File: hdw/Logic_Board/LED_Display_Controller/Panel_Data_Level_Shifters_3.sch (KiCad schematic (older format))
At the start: 43 parts, among them U2801 74LVC1G32, U2802 74HCT541

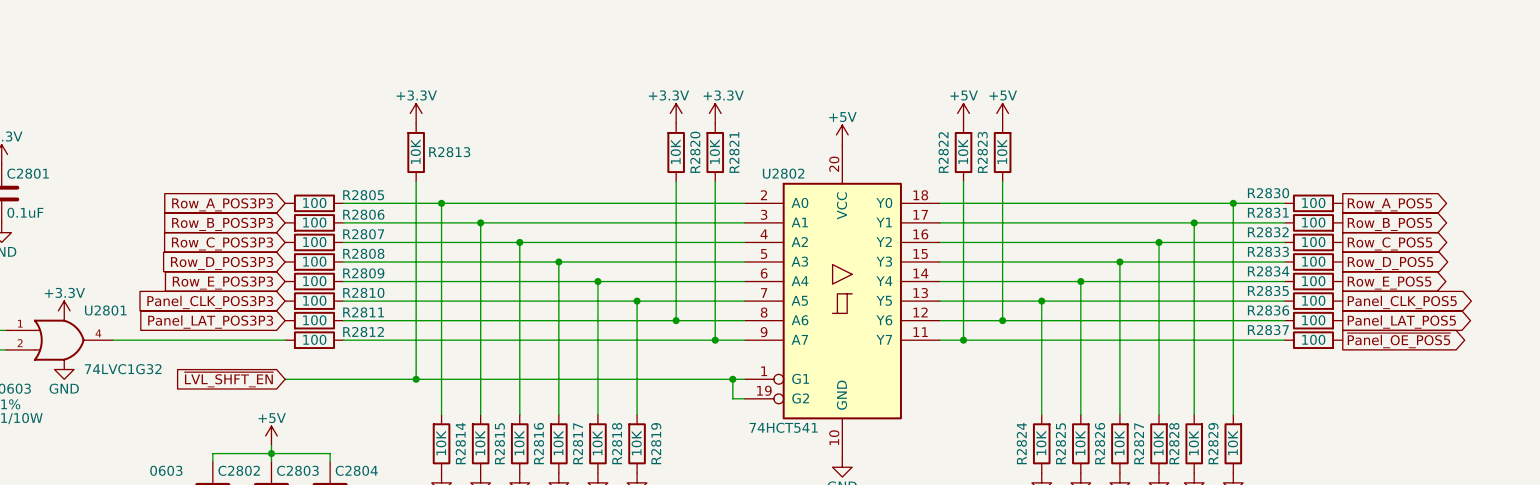
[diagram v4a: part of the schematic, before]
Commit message: Fixed net placement on level shifters, lots of part placements on PCB
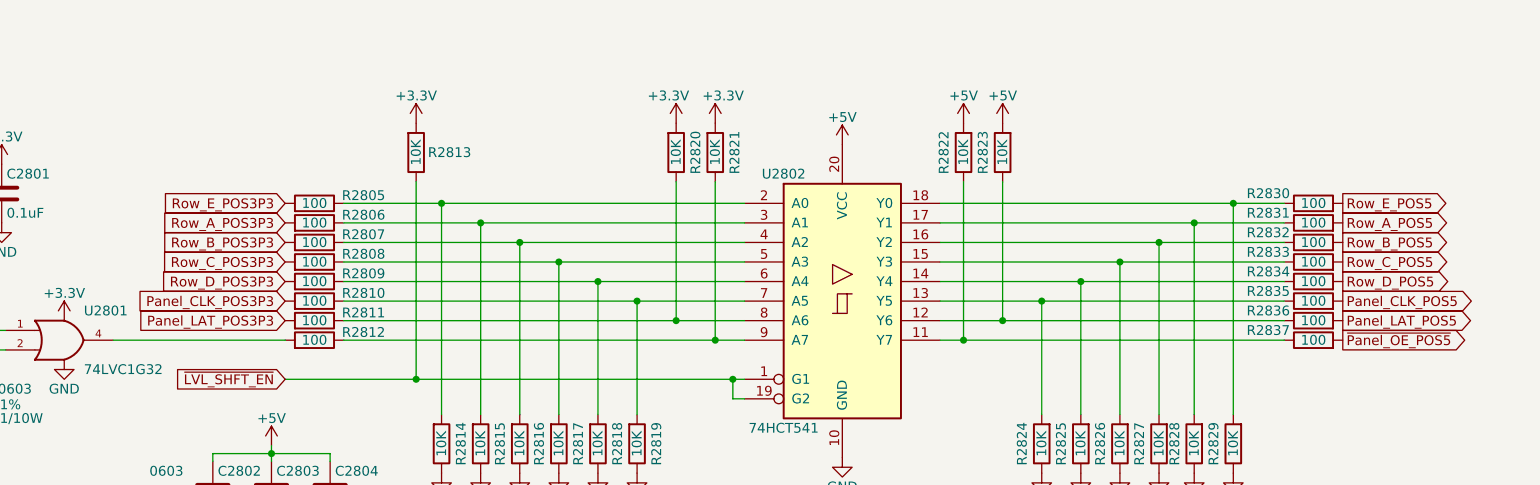
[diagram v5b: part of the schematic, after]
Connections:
- net Row_A_POS3P3: now also R2806.1; no longer R2805.1
- net Row_A_POS5: now also R2831.1; no longer R2830.1
- net Row_B_POS3P3: now also R2807.1; no longer R2806.1
- net Row_B_POS5: now also R2832.1; no longer R2831.1
- net Row_C_POS3P3: now also R2808.1; no longer R2807.1
- net Row_C_POS5: now also R2833.1; no longer R2832.1
- net Row_D_POS3P3: now also R2809.1; no longer R2808.1
- net Row_D_POS5: now also R2834.1; no longer R2833.1
- net Row_E_POS3P3: now also R2805.1; no longer R2809.1
- net Row_E_POS5: now also R2830.1; no longer R2834.1
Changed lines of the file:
@@
 	-1   0    0    -1
 $EndComp
+Text GLabel 9680 3000 2    50   Output ~ 0
+Row_A_POS5
+Text GLabel 9680 3100 2    50   Output ~ 0
+Row_B_POS5
+Text GLabel 9680 3200 2    50   Output ~ 0
+Row_C_POS5
+Text GLabel 9680 3300 2    50   Output ~ 0
+Row_D_POS5
 Text GLabel 9680 2900 2    50   Output ~ 0
-Row_A_POS5
-Text GLabel 9680 3000 2    50   Output ~ 0
-Row_B_POS5
-Text GLabel 9680 3100 2    50   Output ~ 0
-Row_C_POS5
-Text GLabel 9680 3200 2    50   Output ~ 0
-Row_D_POS5
-Text GLabel 9680 3300 2    50   Output ~ 0
 Row_E_POS5
 Text GLabel 9680 3400 2    50   Output ~ 0
@@
 Wire Wire Line
 	4570 3200 5670 3200
+Text GLabel 4270 3000 0    50   Input ~ 0
+Row_A_POS3P3
+Text GLabel 4270 3100 0    50   Input ~ 0
+Row_B_POS3P3
+Text GLabel 4270 3200 0    50   Input ~ 0
+Row_C_POS3P3
+Text GLabel 4270 3300 0    50   Input ~ 0
+Row_D_POS3P3
 Text GLabel 4270 2900 0    50   Input ~ 0
-Row_A_POS3P3
-Text GLabel 4270 3000 0    50   Input ~ 0
-Row_B_POS3P3
-Text GLabel 4270 3100 0    50   Input ~ 0
-Row_C_POS3P3
-Text GLabel 4270 3200 0    50   Input ~ 0
-Row_D_POS3P3
-Text GLabel 4270 3300 0    50   Input ~ 0
 Row_E_POS3P3
 Text GLabel 4270 3400 0    50   Input ~ 0

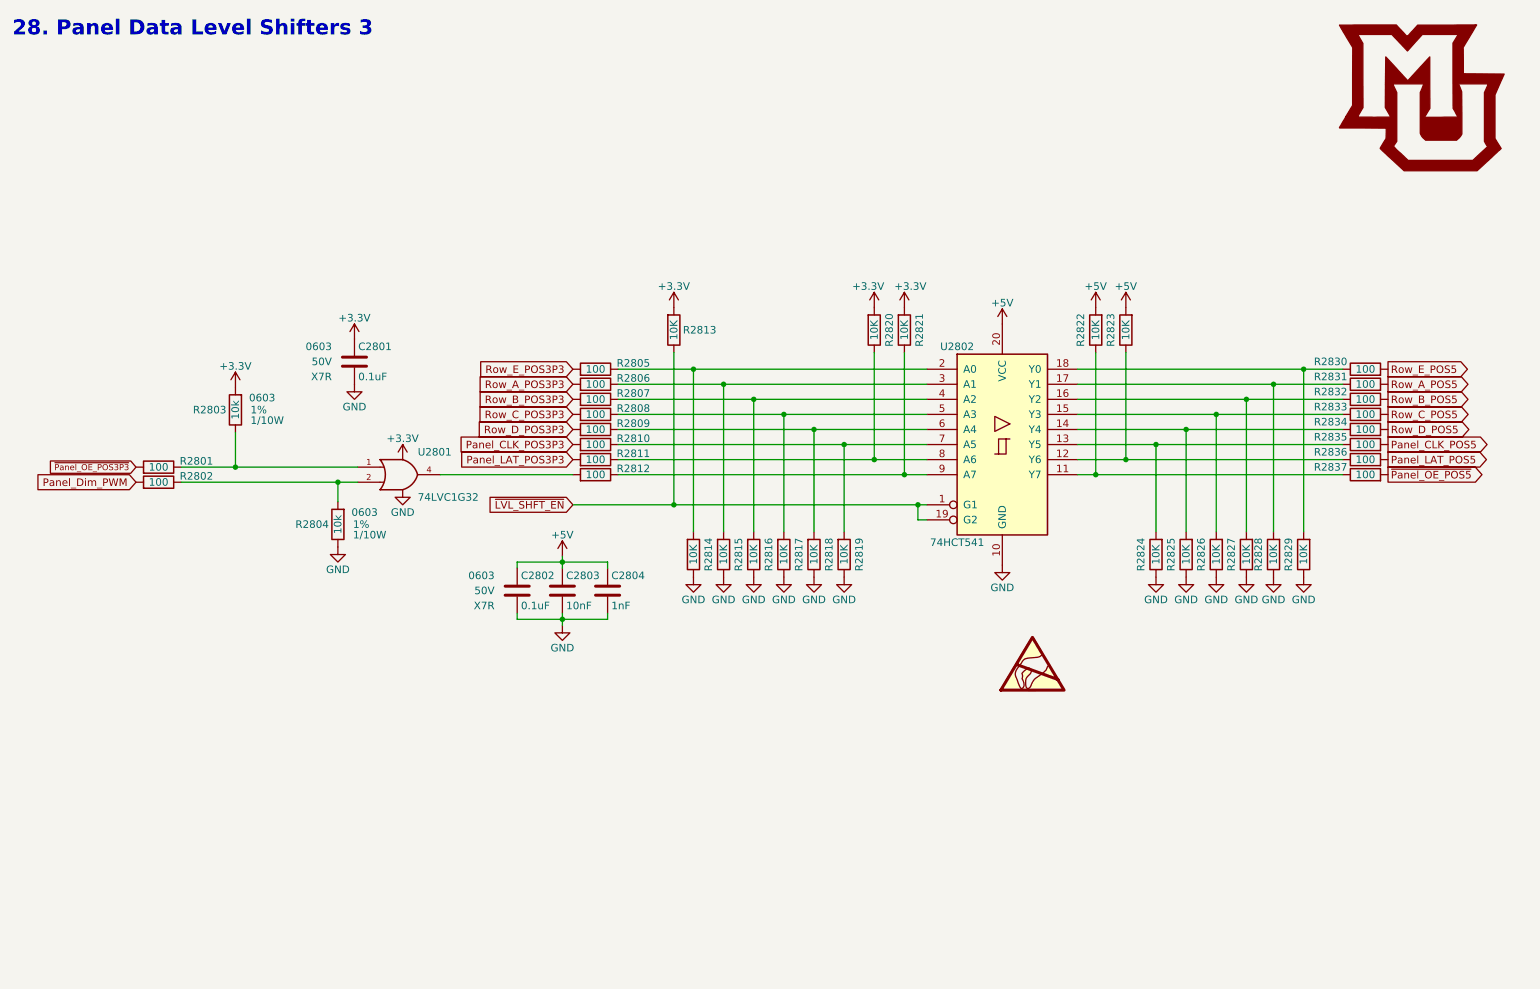
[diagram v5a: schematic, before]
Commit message: Placed more parts, added some labels
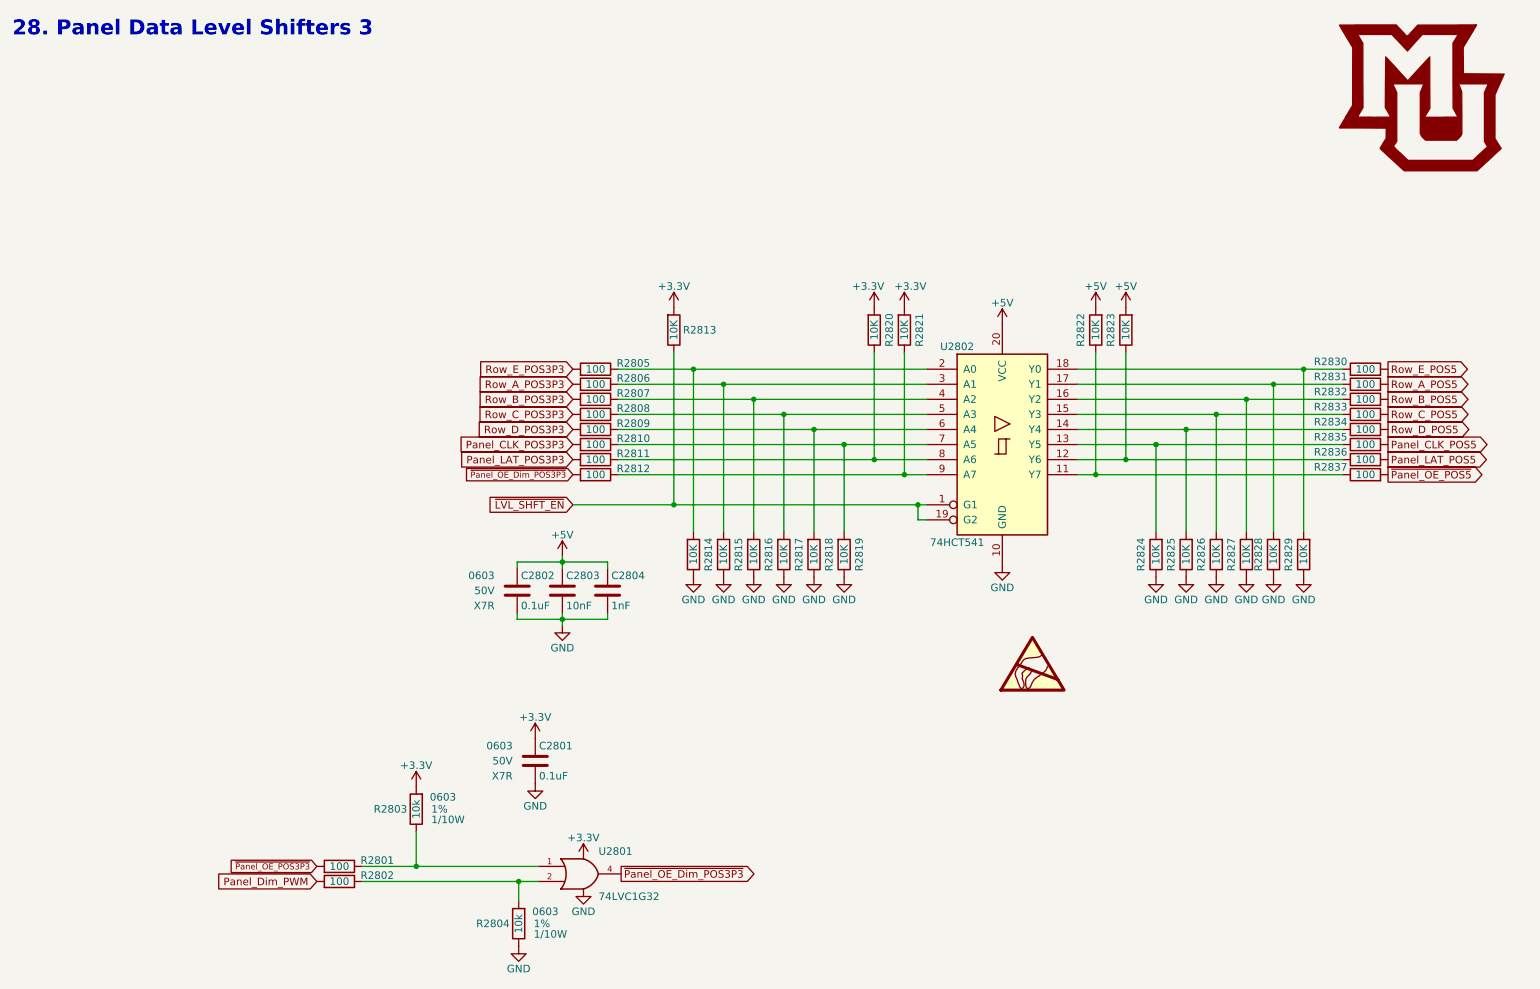
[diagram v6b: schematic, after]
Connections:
- net ~Panel_OE_Dim_POS3P3: now reaches R2812.1, U2801.4
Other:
- moved on the sheet: C2801, R2801, R2802, R2803, R2804, U2801

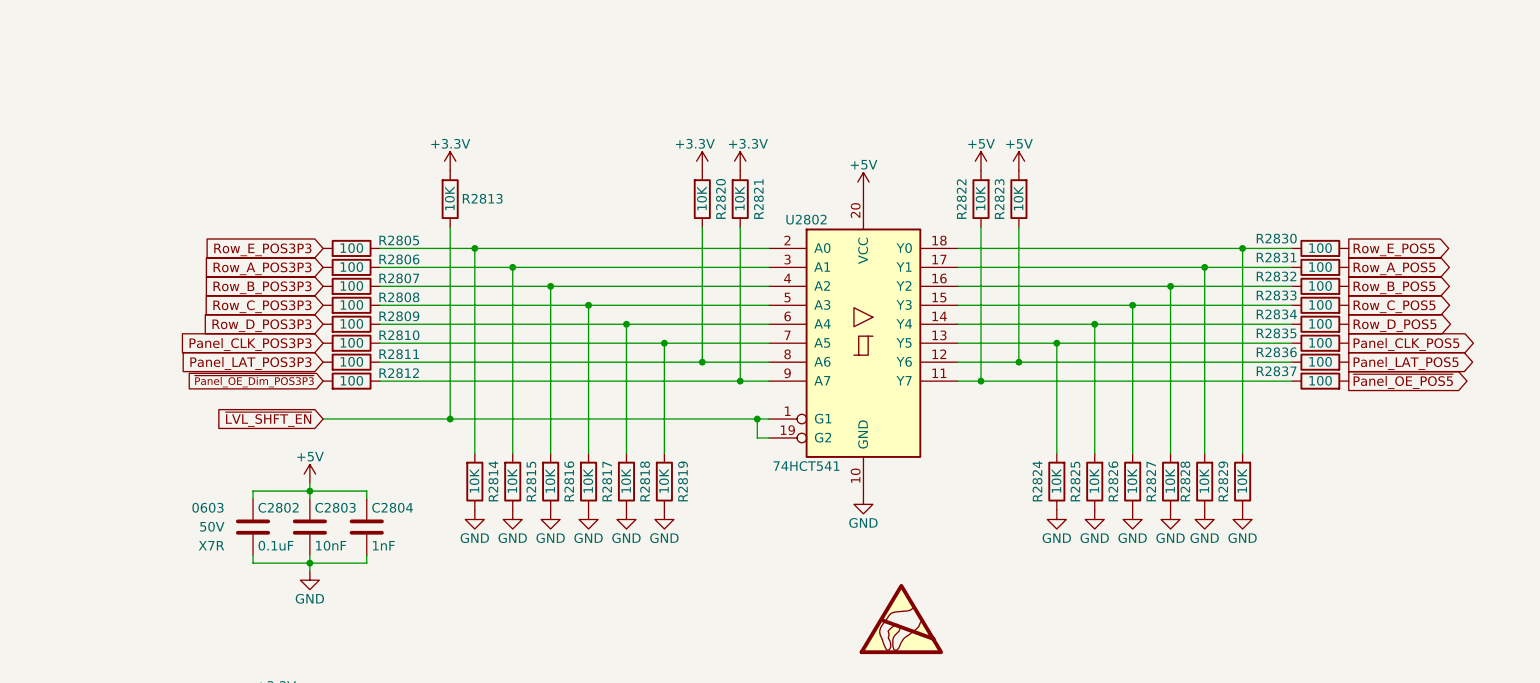
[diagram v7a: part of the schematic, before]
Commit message: Resolved panel data connector orientation issues
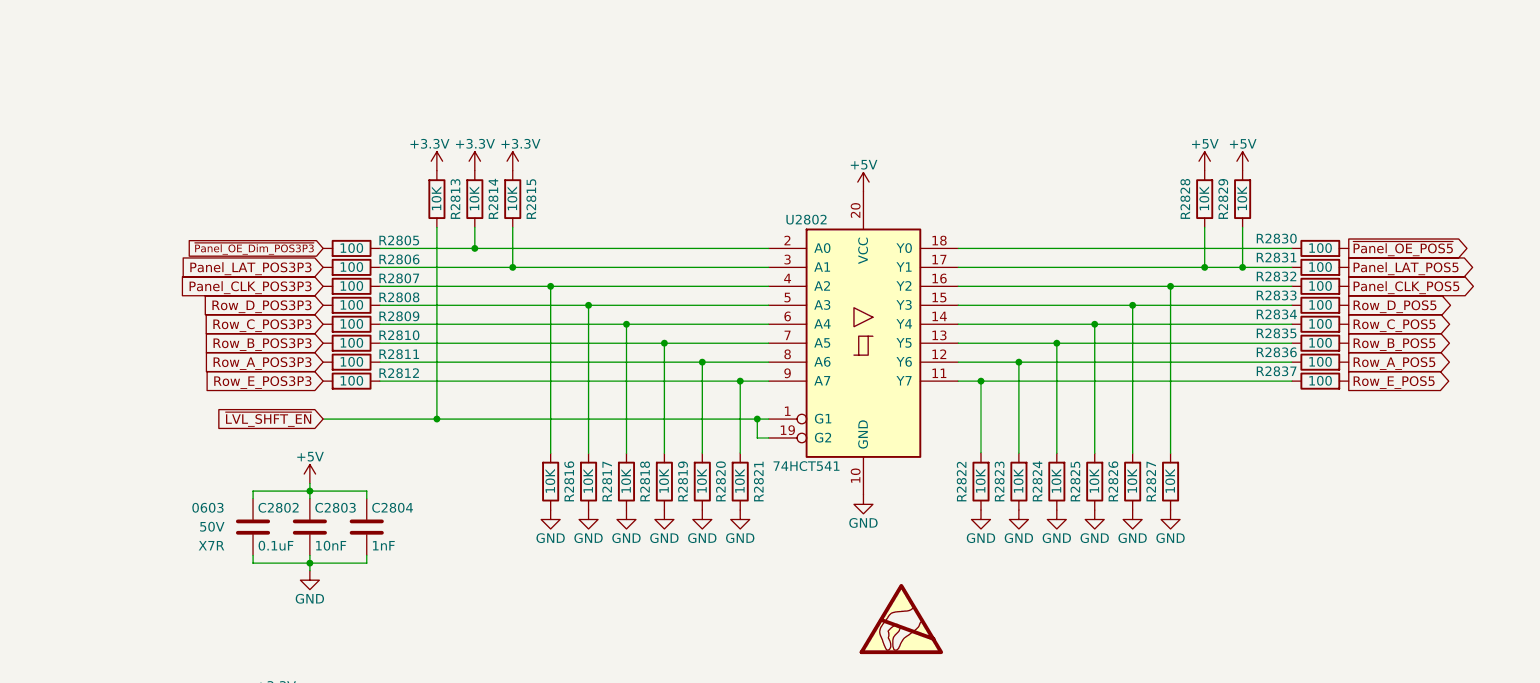
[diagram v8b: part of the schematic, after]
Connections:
- net +3V3: now also R2814.1, R2815.1; no longer R2820.1, R2821.1
- net +5V: now also R2828.1, R2829.1; no longer R2822.1, R2823.1
- net GND: now also R2820.2, R2821.2, R2822.2, R2823.2; no longer R2814.2, R2815.2, R2828.2, R2829.2
- net Panel_CLK_POS3P3: now also R2807.1; no longer R2810.1
- net Panel_CLK_POS5: now also R2832.1; no longer R2835.1
- net Panel_LAT_POS3P3: now also R2806.1; no longer R2811.1
- net Panel_LAT_POS5: now also R2831.1; no longer R2836.1
- net Row_A_POS3P3: now also R2811.1; no longer R2806.1
- net Row_A_POS5: now also R2836.1; no longer R2831.1
- net Row_B_POS3P3: now also R2810.1; no longer R2807.1
- net Row_B_POS5: now also R2835.1; no longer R2832.1
- net Row_C_POS3P3: now also R2809.1; no longer R2808.1
- net Row_C_POS5: now also R2834.1; no longer R2833.1
- net Row_D_POS3P3: now also R2808.1; no longer R2809.1
- net Row_D_POS5: now also R2833.1; no longer R2834.1
- net Row_E_POS3P3: now also R2812.1; no longer R2805.1
- net Row_E_POS5: now also R2837.1; no longer R2830.1
- net ~Panel_OE_Dim_POS3P3: now also R2805.1; no longer R2812.1
- net ~Panel_OE_POS5: now also R2830.1; no longer R2837.1
- net at R2830.2, U2802.18 (Y0): no longer R2829.1
- net at R2806.2, U2802.3 (A1): now also R2815.2; no longer R2815.1
- net at R2805.2, U2802.2 (A0): now also R2814.2; no longer R2814.1
- net at R2811.2, U2802.8 (A6): now also R2820.1; no longer R2820.2
- net at R2812.2, U2802.9 (A7): now also R2821.1; no longer R2821.2
- net at R2836.2, U2802.12 (Y6): now also R2823.1; no longer R2823.2
- net at R2837.2, U2802.11 (Y7): now also R2822.1; no longer R2822.2
- net at R2831.2, U2802.17 (Y1): now also R2828.2, R2829.2; no longer R2828.1
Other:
- moved on the sheet: R2813, R2814, R2815, R2820, R2821, R2822, R2823, R2828, R2829
